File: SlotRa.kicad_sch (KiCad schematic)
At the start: 37 parts, among them J1 Nice!nano - left pins, J10 Battery Holes, J14 GPS Pins, J2 Nice!nano - right pins, J3 ModemL, J4 ModemR, J5 I2C, J6 T1 Drain - SMD, J7 T2 Drain - SMD, J8 T3 Drain - SMD, J9 Battery Connector JST 1.25, SW1 ButRst, SW2 ButUsr, T1 SI2312, T2 SI2312, T3 SI2312, U1 XB8089D0

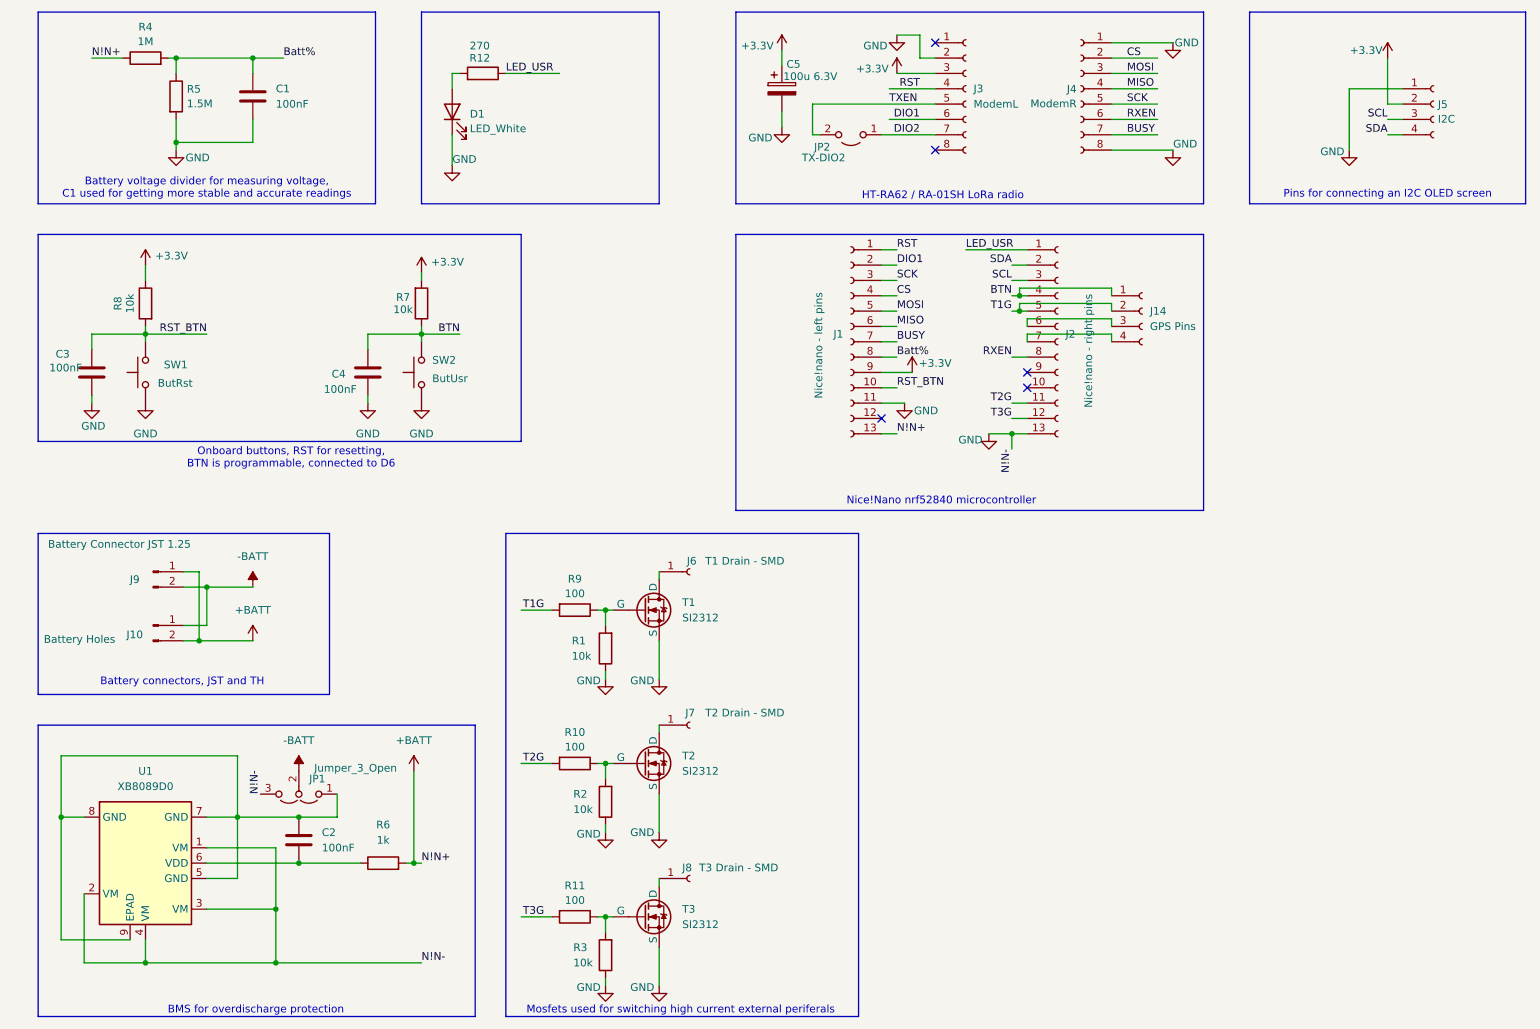
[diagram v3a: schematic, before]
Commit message: Buses renaming, power reconnection
I can't understand why there are labeled connections with creepy names that doubles already existing buses. So, say goodbye to that labels and say hello to clean and logical named bus symbols.
Also renamed Batt-Percent. Looks like some kind of expression, but actually it is indeed a connection to voltage-measuring line. I prefer ADC_BATT for that purpose.
Renamed jumpers' labels.
Deleted one of the battery connectors: no need to use redundancy in this fork.
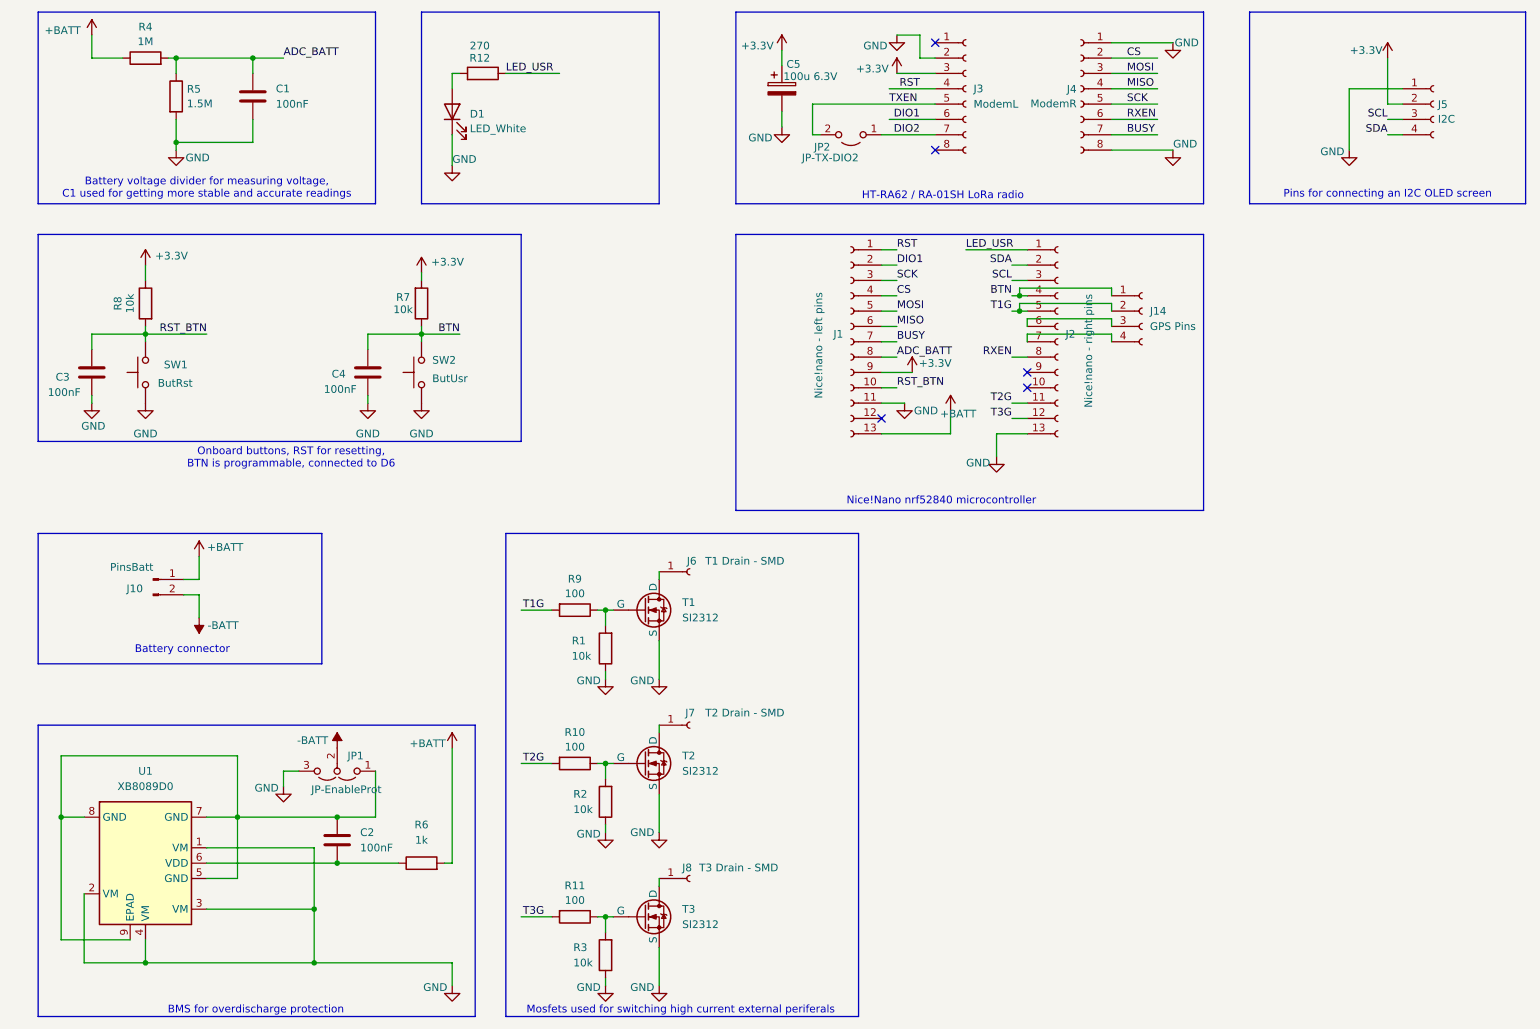
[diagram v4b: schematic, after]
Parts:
- removed J9: Battery Connector JST 1.25, Connector_JST:JST_GH_SM02B-GHS-TB_1x02-1MP_P1.25mm_Horizontal, symbol Connector:Conn_01x02_Pin
- J10: value Battery Holes -> PinsBatt
- JP1: value Jumper_3_Open -> JP-EnableProt
- JP2: value TX-DIO2 -> JP-TX-DIO2
- SW2: footprint Button_Switch_SMD:SW_Push_SPST_NO_Alps_SKRK -> Connector_PinHeader_2.54mm:PinHeader_1x02_P2.54mm_Vertical
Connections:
- net +BATT: now also J10.1 (Pin_1); no longer J10.2 (Pin_2)
- net -BATT: now also J10.2 (Pin_2); no longer J10.1 (Pin_1)
- net Batt% renamed ADC_BATT
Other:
- note added: "Battery connector"
- note removed: "Battery connectors, JST and TH"
- moved on the sheet: C2, J10, JP1, R6

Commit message: GPS port and uC-PCB schematics
And now the PCB's pin-headers become readable in the schematics.
GPS's pins are separated, I dunno why they used 4-pin pads with attached user button, but no power buses at all. Now there are 5-pin pads with mandatory power and data lines and an optional enable signal.
Removed the first power mosfet that also could regulate GPS's power. Let's make it something external. What if the GPS unit already has EN signal?
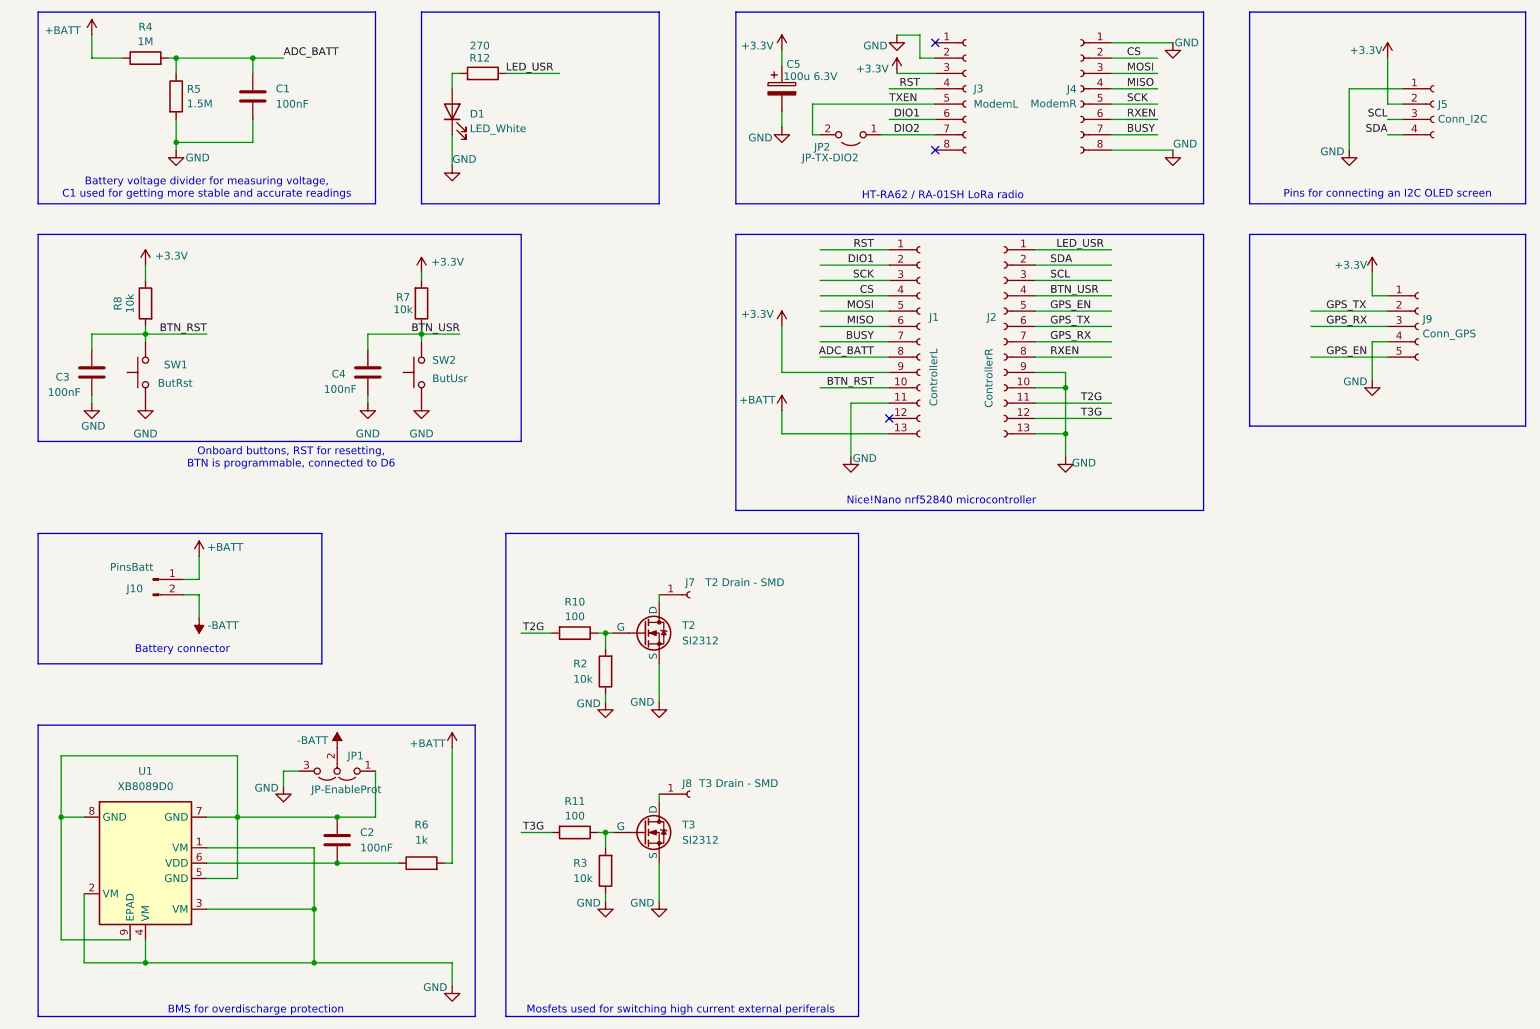
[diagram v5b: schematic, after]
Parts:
- removed J14: GPS Pins, SMD_PAD:SMD_PAD_4x1, symbol Connector:Conn_01x04_Socket
- removed J6: T1 Drain - SMD, SMD_PAD:SMD_PAD_1x1, symbol Connector:Conn_01x01_Socket
- removed R1: 10k, Resistor_SMD:R_0805_2012Metric_Pad1.20x1.40mm_HandSolder, symbol Device:R
- removed R9: 100, Resistor_SMD:R_0805_2012Metric_Pad1.20x1.40mm_HandSolder, symbol Device:R
- removed T1: SI2312, SMD_PAD:TSOT-23_HandSoldering_Updated, symbol Simulation_SPICE:NMOS
- added J9: Conn_GPS, Connector_Wire:SolderWire-0.1sqmm_1x05_P3.6mm_D0.4mm_OD1mm, symbol Connector:Conn_01x05_Socket
- J1: value Nice!nano - left pins -> ControllerL
- J2: value Nice!nano - right pins -> ControllerR
- J5: value I2C -> Conn_I2C
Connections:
- net +3.3V: now also J9.1 (Pin_1)
- net GND: now also J2.10 (Pin_10), J2.9 (Pin_9), J9.4 (Pin_4)
- net GPS_TX: now reaches J2.6 (Pin_6)
- net GPS_TX: now also J9.2 (Pin_2)
- net GPS_RX: now reaches J2.7 (Pin_7)
- net GPS_RX: now also J9.3 (Pin_3)
- net BTN renamed BTN_USR
- net RST_BTN renamed BTN_RST
- net T1G renamed GPS_EN
- net GPS_EN: now also J9.5 (Pin_5)
- no-connect marks 5 -> 3
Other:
- moved on the sheet: J1, J2, J7, J8, R10, R11, R2, R3, T2, T3

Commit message: Transistors purging and more adjustments
And now there is only one power MOSFET. One can connect it to a vibromotor, for example. Also it uses pin-header with 2 pins: 1 connected to a battery line and one - to the MOSFET.
There are also some minor schematic and symbols adjustments.
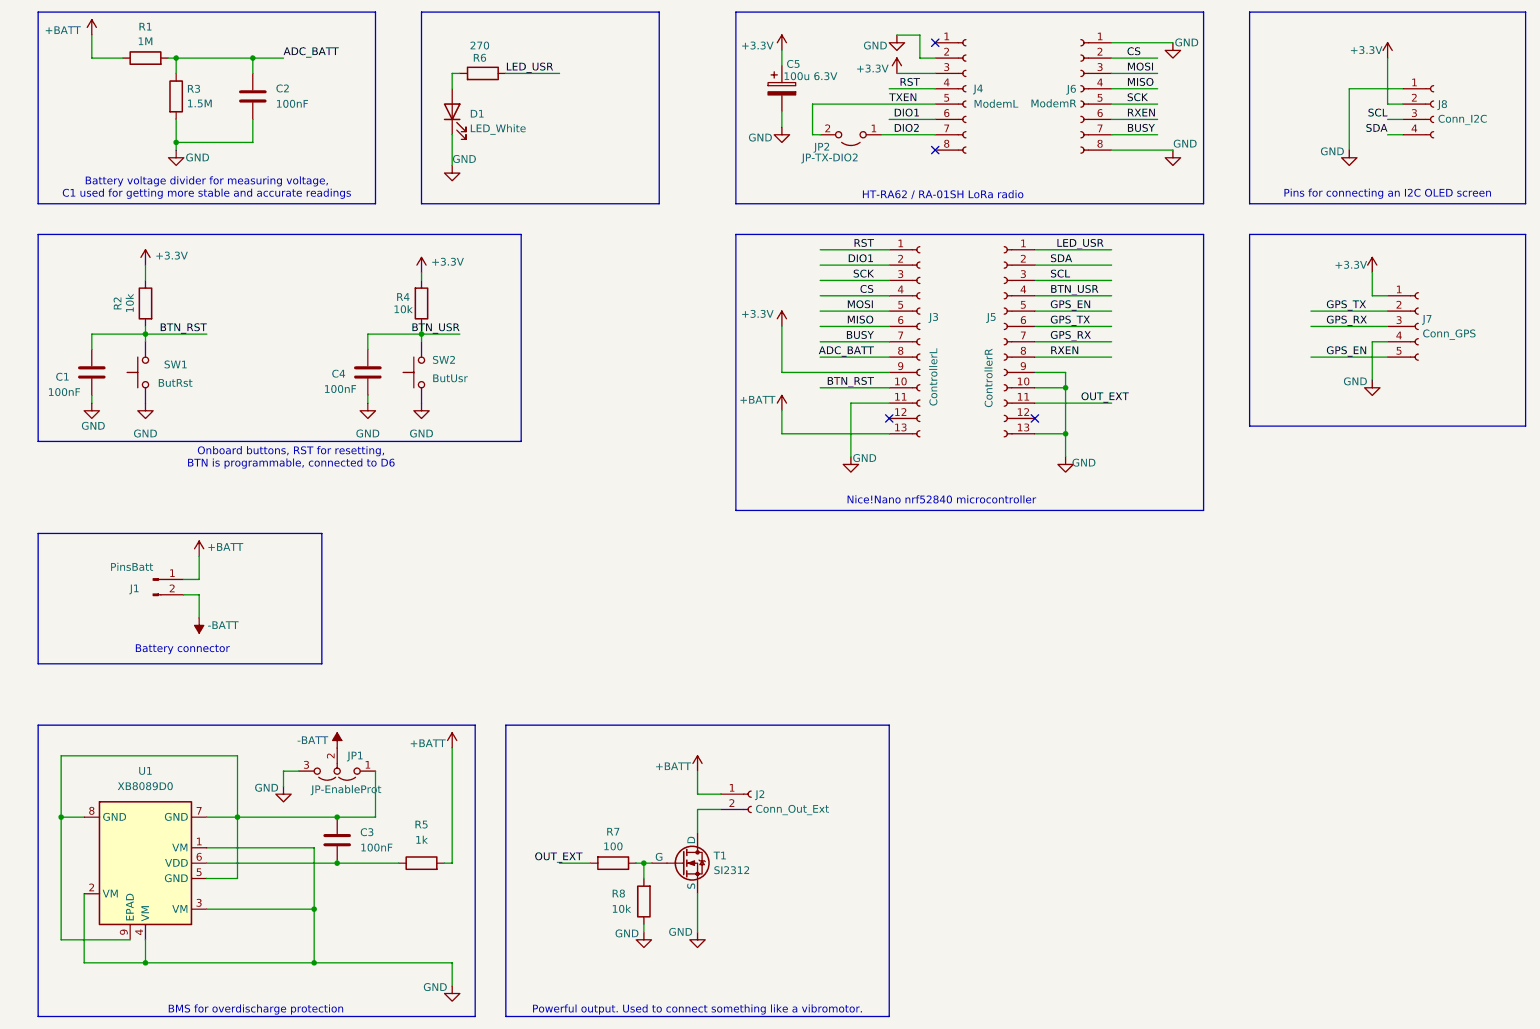
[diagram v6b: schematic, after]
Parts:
- removed J7: T2 Drain - SMD, SMD_PAD:SMD_PAD_1x1, symbol Connector:Conn_01x01_Socket
- removed J8: T3 Drain - SMD, SMD_PAD:SMD_PAD_1x1, symbol Connector:Conn_01x01_Socket
- removed R11: 100, Resistor_SMD:R_0805_2012Metric_Pad1.20x1.40mm_HandSolder, symbol Device:R
- removed R3: 10k, Resistor_SMD:R_0805_2012Metric_Pad1.20x1.40mm_HandSolder, symbol Device:R
- removed T3: SI2312, SMD_PAD:TSOT-23_HandSoldering_Updated, symbol Simulation_SPICE:NMOS
- added J2: Conn_Out_Ext, Connector_PinHeader_2.54mm:PinHeader_1x02_P2.54mm_Vertical, symbol Connector:Conn_01x02_Socket
- J7: renamed from J9; footprint Connector_Wire:SolderWire-0.1sqmm_1x05_P3.6mm_D0.4mm_OD1mm -> Connector_PinHeader_2.00mm:PinHeader_1x05_P2.00mm_Vertical
- renumbered C3 to C1, C1 to C2, C2 to C3, J10 to J1, J1 to J3, J3 to J4, J2 to J5, J4 to J6, J5 to J8, R4 to R1, R8 to R2, R5 to R3, R7 to R4, R6 to R5, R12 to R6, R10 to R7, R2 to R8, T2 to T1
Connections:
- net +BATT: now also J2.1 (Pin_1)
- net at T1.1 (D): now also J2.2 (Pin_2)
- net T2G renamed OUT_EXT
- net T3G: no longer names the net of J5.12 (Pin_12)
- no-connect marks 3 -> 4
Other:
- note added: "Powerful output. Used to connect something like a vibromotor."
- note removed: "Mosfets used for switching high current external periferals"
- moved on the sheet: R7, R8, T1

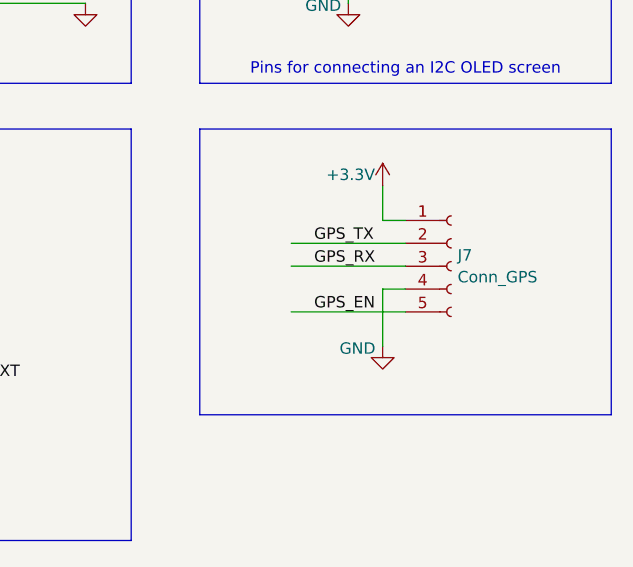
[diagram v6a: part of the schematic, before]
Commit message: Finally, The PCB
Small fixes in the schematics.
Recreated the PCB. A toucght one, there were too many wrong decisions that led to a non-upgradability of the project without the Power Of Some Mother And The Sledgehammer.
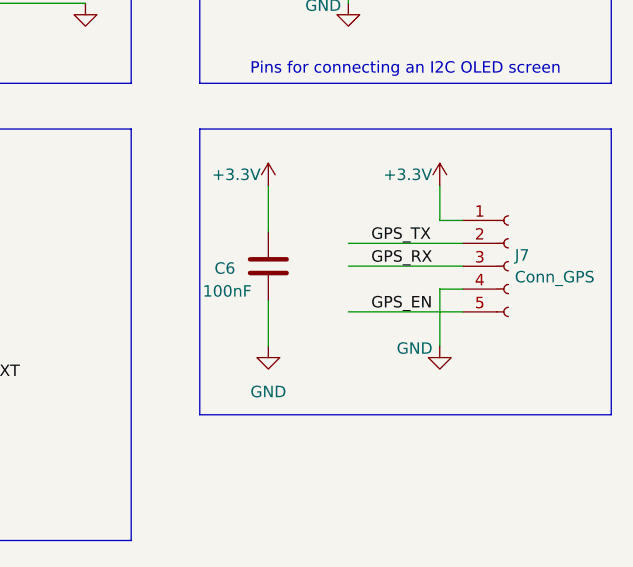
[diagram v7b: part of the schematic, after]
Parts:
- added C6: 100nF, Capacitor_SMD:C_0805_2012Metric_Pad1.18x1.45mm_HandSolder, symbol Device:C
- J3, J5: footprint SMD_PAD:SMD_Pad_Row_P2.54_13x1 -> SlotRa:SMD_Pad_Row_P2.54_13x1
- J4: footprint SMD_PAD:SMD_Pad_Row_P2.00_8x1_longer -> SlotRa:SMD_Pad_Row_P2.00_8x1_longer
- J6: footprint SMD_PAD:SMD_Pad_Row_P2.00_8x1 -> SlotRa:SMD_Pad_Row_P2.00_8x1
- SW1: footprint Button_Switch_SMD:SW_Push_SPST_NO_Alps_SKRK -> SlotRa:KLS7-TS6335
- T1: footprint SMD_PAD:TSOT-23_HandSoldering_Updated -> SlotRa:TSOT-23_HandSoldering_Updated
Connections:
- net +3.3V: now also C6.2
- net GND: now also C6.1
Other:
- moved on the sheet: J7
